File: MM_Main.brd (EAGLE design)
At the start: 74 x 87.2 mm, 81 parts, among them IC1 ULN2003AD, IC2 TB6612FNG, IC4 LD117ADT50TR, IC5 MCP1825, Q1 TEFT4300, Q2 TEFT4300, Q3 TEFT4300, Q4 TEFT4300, Q5 TEFT4300, Q6 TEFT4300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

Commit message: poprawione przyciski, kwarc i wylacznik zasilania
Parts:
- removed BT0, BT1, RST_BTN: TACTILE-SWITCH-7914G, GeekAmmo:7914G
- removed ZAS: (no value), special:EDG-01
- added Q8: 8MHz, _microMouse:CRYSTAL_5X3.2MM
- added S1: TL32PO, switch:TL3XPO
- added S2, S3: DTS-3, switch-tact:DTS-3
- added S4: DTSM-6, switch-tact:DTSM-6
- added S5: DTSM-3, switch-tact:DTSM-3
- added U$2: CRYSTAL_5X3.2MM, _microMouse:CRYSTAL_5X3.2MM
- C_OSC1, C_OSC2: value 27p -> 33p
- LED4: value green -> blue
- LED6: value yellow -> blue
- R10, R12, R13: value 10K -> 150R
- R11: value 10K -> 10k
- R20, R27: value 10K -> 33R
- R25: value (none) -> 10k
- moved Q7 37.0 mm to (42.6, 31.5)
- moved FUSE 13.6 mm to (-22.8, -32.2), turned to 180 degrees
- moved FUSE1 10.9 mm to (-22.8, -30.0), turned to 180 degrees
- moved LED3 4.58 mm to (28.4, -30.8), turned to 25 degrees
- moved LED2 2.01 mm to (29.2, -23.3), turned to 270 degrees
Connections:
- net +3V3: now also S3.1; no longer BT0.3
- net BTN: now also S2.1; no longer BT1.3
- net GND: now also S5.1; no longer RST_BTN.3
- net N$23: now also S3.2; no longer BT0.1
- net N$24: now also S1.2; no longer ZAS.2
- net N$29: now also S2.2; no longer BT1.1
- net N$9: now also S1.3; no longer ZAS.1
- net OSC_IN: now also Q8.P$2; no longer Q7.3
- net OSC_OUT: now also Q8.P$1; no longer Q7.1
- net RST: now also S5.2; no longer RST_BTN.1
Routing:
- net +7V: track 88.7 -> 75.3 mm
- net N$21: track 31.8 -> 24.8 mm
- net +3V3: track 345.6 -> 350.9 mm
- net N$23: track 32.6 -> 37.9 mm
- net N$24: track 5.84 -> 11.0 mm
- net LED2: track 59.5 -> 63.7 mm
- net BTN: track 71.8 -> 75.6 mm
- net OSC_IN: track 20.8 -> 17.6 mm, vias 2 -> 0
- net N$9: track 11.8 -> 8.63 mm
- net GND: track 468.3 -> 465.3 mm, vias 22 -> 20
- net N$8: track 22.5 -> 24.0 mm
- net LED1: track 57.1 -> 58.5 mm
- net N$29: track 25.2 -> 26.3 mm
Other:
- outline, holes or cut-outs redrawn
- board text removed: "BT0"
- board text removed: "BT1"
- board text removed: "BUZ1"
- board text removed: "C1"
- board text removed: "C12"
- board text removed: "C13"
- board text removed: "C15"
- board text removed: "C2"
- board text removed: "C21"
- board text removed: "C22"
- board text removed: "C3"
- board text removed: "C6"
- board text removed: "C_OSC1"
- board text removed: "C_OSC2"
- board text removed: "C_V1"
- board text removed: "C_V2"
- board text removed: "C_V3"
- board text removed: "C_VSSA"
- board text removed: "C_VSSA1"
- board text removed: "FUSE"
- board text removed: "IC1"
- board text removed: "IC2"
- board text removed: "IC4"
- board text removed: "IC5"
- board text removed: "LED1"
- board text removed: "LED2"
- board text removed: "LED3"
- board text removed: "LED4"
- board text removed: "LED6"
- board text removed: "R1"
- board text removed: "R10"
- board text removed: "R11"
- board text removed: "R12"
- board text removed: "R13"
- board text removed: "R15"
- board text removed: "R16"
- board text removed: "R17"
- board text removed: "R18"
- board text removed: "R19"
- board text removed: "R2"
- board text removed: "R20"
- board text removed: "R21"
- board text removed: "R22"
- board text removed: "R23"
- board text removed: "R24"
- board text removed: "R25"
- board text removed: "R26"
- board text removed: "R27"
- board text removed: "R3"
- board text removed: "R4"
- board text removed: "R5"
- board text removed: "R6"
- board text removed: "R7"
- board text removed: "R8"
- board text removed: "R9"
- board text removed: "RST_BTN"
- board text removed: "VCAP_1"
- board text removed: "VCAP_2"
- board text removed: "ZAS"

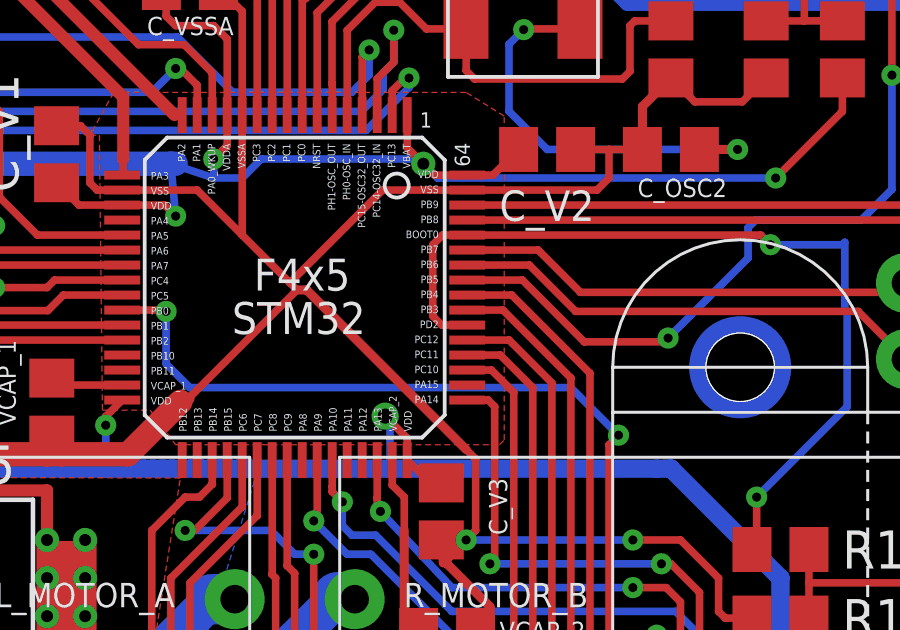
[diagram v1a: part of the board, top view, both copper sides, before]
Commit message: PD2 zamienione z PA15
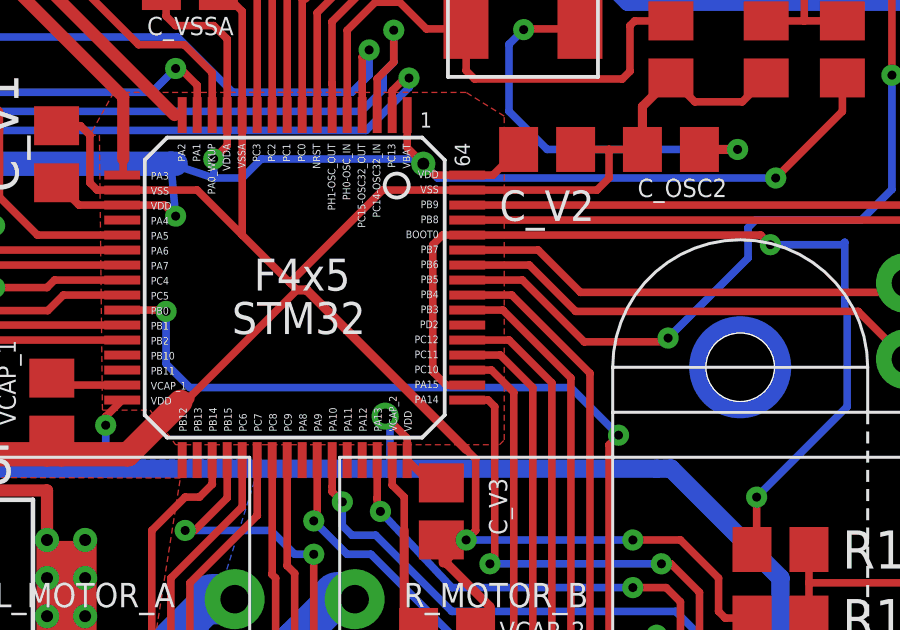
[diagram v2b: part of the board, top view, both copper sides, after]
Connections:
- net BOOT0: now also U$6.PA15; no longer U$6.PD2
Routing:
- net BOOT0: track 29.3 -> 31.2 mm
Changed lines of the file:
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@@
 <wire x1="5.75" y1="13.33875" x2="15.5347" y2="13.33875" width="0.254" layer="1"/>
 <wire x1="15.5347" y1="13.33875" x2="15.85595" y2="13.0175" width="0.254" layer="1"/>
-<contactref element="U$6" pad="PD2"/>
 <wire x1="5.75" y1="13.33875" x2="4.925" y2="13.33875" width="0.254" layer="1"/>
 <wire x1="4.925" y1="13.33875" x2="4.60375" y2="13.0175" width="0.254" layer="1"/>
-<wire x1="5.75" y1="10.33875" x2="4.90125" y2="10.33875" width="0.254" layer="1"/>
-<wire x1="4.90125" y1="10.33875" x2="4.60375" y2="10.63625" width="0.254" layer="1"/>
-<wire x1="4.60375" y1="10.63625" x2="4.60375" y2="13.0175" width="0.254" layer="1"/>
+<wire x1="4.60375" y1="8.78205" x2="4.60375" y2="13.0175" width="0.254" layer="1"/>
 <wire x1="15.2425" y1="2.8575" x2="15.39875" y2="3.01375" width="0.254" layer="1"/>
 <wire x1="15.39875" y1="3.01375" x2="15.39875" y2="4.60375" width="0.254" layer="1"/>
@@
 <wire x1="18.415" y1="10.795" x2="18.335625" y2="10.874375" width="0.254" layer="16"/>
 <wire x1="18.335625" y1="10.874375" x2="18.335625" y2="13.096875" width="0.254" layer="16"/>
+<contactref element="U$6" pad="PA15"/>
+<wire x1="5.75" y1="8.33875" x2="5.75" y2="8.3312" width="0.254" layer="1"/>
+<wire x1="5.75" y1="8.3312" x2="5.0546" y2="8.3312" width="0.254" layer="1"/>
+<wire x1="5.0546" y1="8.3312" x2="4.60375" y2="8.78205" width="0.254" layer="1"/>
 </signal>
 <signal name="N$23">

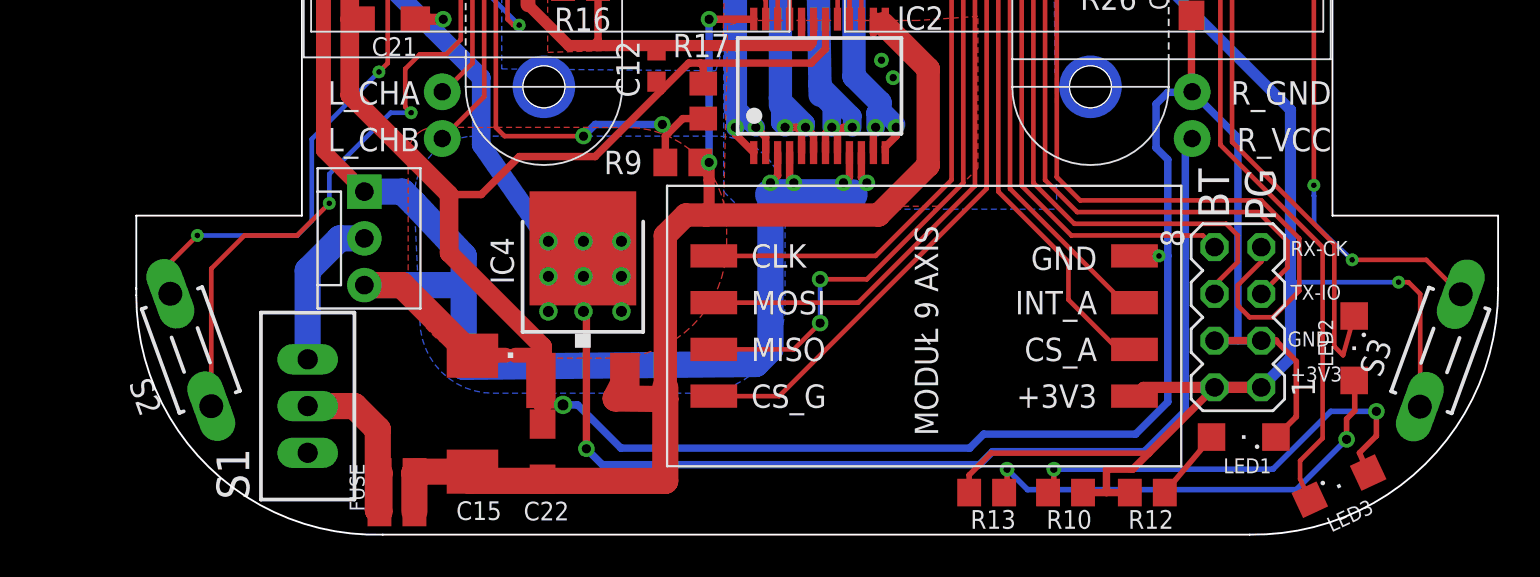
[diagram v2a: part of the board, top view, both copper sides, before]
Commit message: dodany suwak i miejsce na 2 lipo
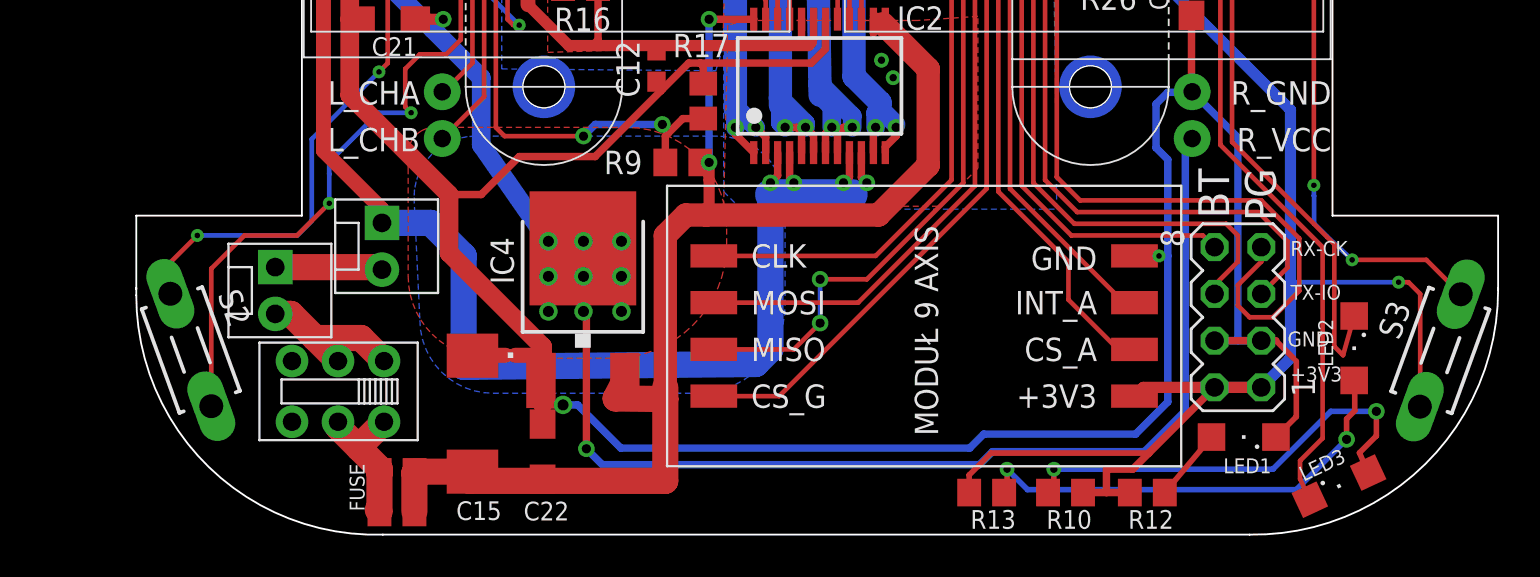
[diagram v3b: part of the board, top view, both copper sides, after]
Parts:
- removed JP1: (no value), SparkFun-Connectors:MOLEX-1X3
- removed S1: TL32PO, switch:TL3XPO
- added JP3, JP4: (no value), SparkFun_conn:MOLEX-1X2
- added U$3: PRZELACZNIK_SUWAKOWY, _microMouse:PRZELACZNIK_SUWAKOWY
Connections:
- new net N$36: JP3.2, U$3.2, U$3.3
- net GNDA: now also JP4.1; no longer JP1.1, JP1.3
- net N$24: now also U$3.5, U$3.6; no longer S1.2
- net N$9: now also JP3.1, JP4.2; no longer JP1.2, S1.3
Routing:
- net GNDA: track 116.6 -> 104.2 mm
- net N$36: track 0.00 -> 8.74 mm
- net N$24: track 11.0 -> 7.95 mm
- net N$9: track 8.63 -> 5.85 mm

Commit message: gerbery
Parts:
- removed Q7: 8MHz, crystal:CTS406
- removed S4: DTSM-6, switch-tact:DTSM-6
- removed U$2: CRYSTAL_5X3.2MM, _microMouse:CRYSTAL_5X3.2MM
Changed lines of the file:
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@@
 <grid distance="10" unitdist="mil" unit="mil" style="lines" multiple="1" display="yes" altdistance="1" altunitdist="mil" altunit="mil"/>
 <layers>
-<layer number="1" name="Top" color="4" fill="1" visible="yes" active="yes"/>
+<layer number="1" name="Top" color="4" fill="1" visible="no" active="yes"/>
 <layer number="2" name="Route2" color="1" fill="3" visible="no" active="no"/>
 <layer number="3" name="Route3" color="4" fill="3" visible="no" active="no"/>
@@
 <layer number="14" name="Route14" color="1" fill="6" visible="no" active="no"/>
 <layer number="15" name="Route15" color="4" fill="6" visible="no" active="no"/>
-<layer number="16" name="Bottom" color="1" fill="1" visible="yes" active="yes"/>
-<layer number="17" name="Pads" color="2" fill="1" visible="yes" active="yes"/>
-<layer number="18" name="Vias" color="2" fill="1" visible="yes" active="yes"/>
-<layer number="19" name="Unrouted" color="6" fill="1" visible="yes" active="yes"/>
-<layer number="20" name="Dimension" color="15" fill="1" visible="yes" active="yes"/>
+<layer number="16" name="Bottom" color="1" fill="1" visible="no" active="yes"/>
+<layer number="17" name="Pads" color="2" fill="1" visible="no" active="yes"/>
+<layer number="18" name="Vias" color="2" fill="1" visible="no" active="yes"/>
+<layer number="19" name="Unrouted" color="6" fill="1" visible="no" active="yes"/>
+<layer number="20" name="Dimension" color="15" fill="1" visible="no" active="yes"/>
 <layer number="21" name="tPlace" color="7" fill="1" visible="yes" active="yes"/>
-<layer number="22" name="bPlace" color="7" fill="1" visible="yes" active="yes"/>
-<layer number="23" name="tOrigins" color="15" fill="1" visible="yes" active="yes"/>
-<layer number="24" name="bOrigins" color="15" fill="1" visible="yes" active="yes"/>
+<layer number="22" name="bPlace" color="7" fill="1" visible="no" active="yes"/>
+<layer number="23" name="tOrigins" color="15" fill="1" visible="no" active="yes"/>
+<layer number="24" name="bOrigins" color="15" fill="1" visible="no" active="yes"/>
 <layer number="25" name="tNames" color="7" fill="1" visible="yes" active="yes"/>
-<layer number="26" name="bNames" color="7" fill="1" visible="yes" active="yes"/>
-<layer number="27" name="tValues" color="7" fill="1" visible="yes" active="yes"/>
-<layer number="28" name="bValues" color="7" fill="1" visible="yes" active="yes"/>
+<layer number="26" name="bNames" color="7" fill="1" visible="no" active="yes"/>
+<layer number="27" name="tValues" color="7" fill="1" visible="no" active="yes"/>
+<layer number="28" name="bValues" color="7" fill="1" visible="no" active="yes"/>
 <layer number="29" name="tStop" color="7" fill="3" visible="no" active="yes"/>
 <layer number="30" name="bStop" color="7" fill="6" visible="no" active="yes"/>
@@
 <element name="Q4" library="_MM" package="TEFT4300" value="TEFT4300" x="3.33375" y="49.05375" smashed="yes" rot="R308"/>
 <element name="Q3" library="_MM" package="TEFT4300" value="TEFT4300" x="-3.33375" y="49.05375" smashed="yes" rot="R52"/>
-<element name="Q7" library="crystal" package="CTS406" value="8MHz" x="42.62" y="31.4945" smashed="yes" rot="R180">
-<attribute name="OC_NEWARK" value="unknown" x="42.62" y="31.4945" size="1.778" layer="27" rot="R180" display="off"/>
-<attribute name="MPN" value="" x="42.62" y="31.4945" size="1.778" layer="27" rot="R180" display="off"/>
-<attribute name="MF" value="" x="42.62" y="31.4945" size="1.778" layer="27" rot="R180" display="off"/>
-<attribute name="OC_FARNELL" value="unknown" x="42.62" y="31.4945" size="1.778" layer="27" rot="R180" display="off"/>
-<attribute name="VALUE" x="45.16" y="35.3045" size="1.27" layer="27" rot="R180"/>
-</element>
 <element name="R1" library="rcl" package="R0805" value="" x="20.5994" y="25.48255" smashed="yes" rot="R180">
 <attribute name="NAME" x="18.85315" y="26.11755" size="1.27" layer="25" rot="R180"/>
@@
 <attribute name="VALUE" x="15.5575" y="-4.1275" size="1.27" layer="27"/>
 </element>
-<element name="U$2" library="_microMouse" package="CRYSTAL_5X3.2MM" value="CRYSTAL_5X3.2MM" x="-265.18405" y="0"/>
 <element name="Q8" library="_microMouse" package="CRYSTAL_5X3.2MM" value="8MHz" x="7.4092" y="20.0818"/>
 <element name="S2" library="switch-tact" package="DTS-3" value="DTS-3" x="-34.036" y="-23.368" smashed="yes" rot="R110">
@@
 <attribute name="VALUE" x="37.839696875" y="-27.591315625" size="1.27" layer="27" rot="R70" display="off"/>
 </element>
-<element name="S4" library="switch-tact" package="DTSM-6" value="DTSM-6" x="37.338" y="45.212"/>
 <element name="S5" library="switch-tact" package="DTSM-3" value="DTSM-3" x="0" y="24.13"/>
 <element name="JP3" library="SparkFun_conn" package="MOLEX-1X2" value="" x="-29.4492" y="-18.8658" smashed="yes" rot="R270"/>

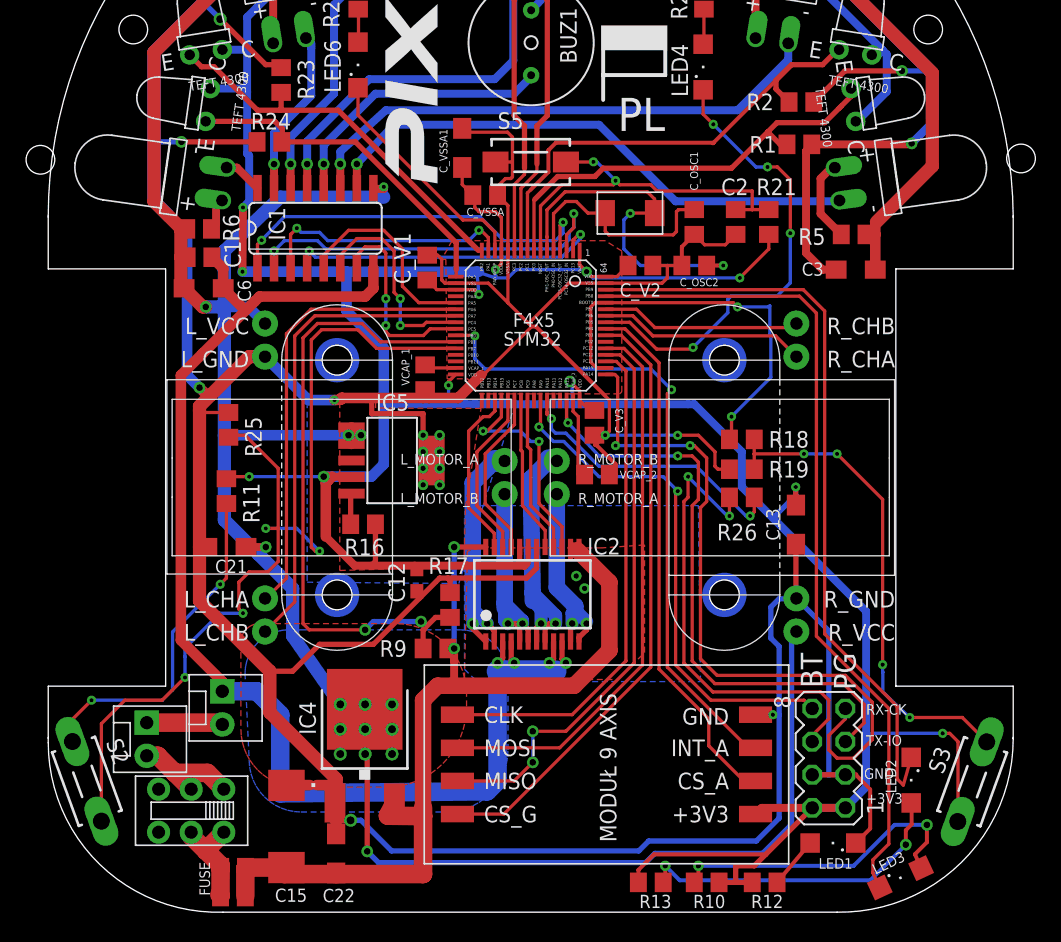
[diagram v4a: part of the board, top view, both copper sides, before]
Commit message: to 2 gniazdo moze szorowac o kolo... zmienilem tez konfiguuracje power-switcha, bo tak patrzac na strone electro-parku to tak odczyruje ta konfiguracje, zrobilem drc
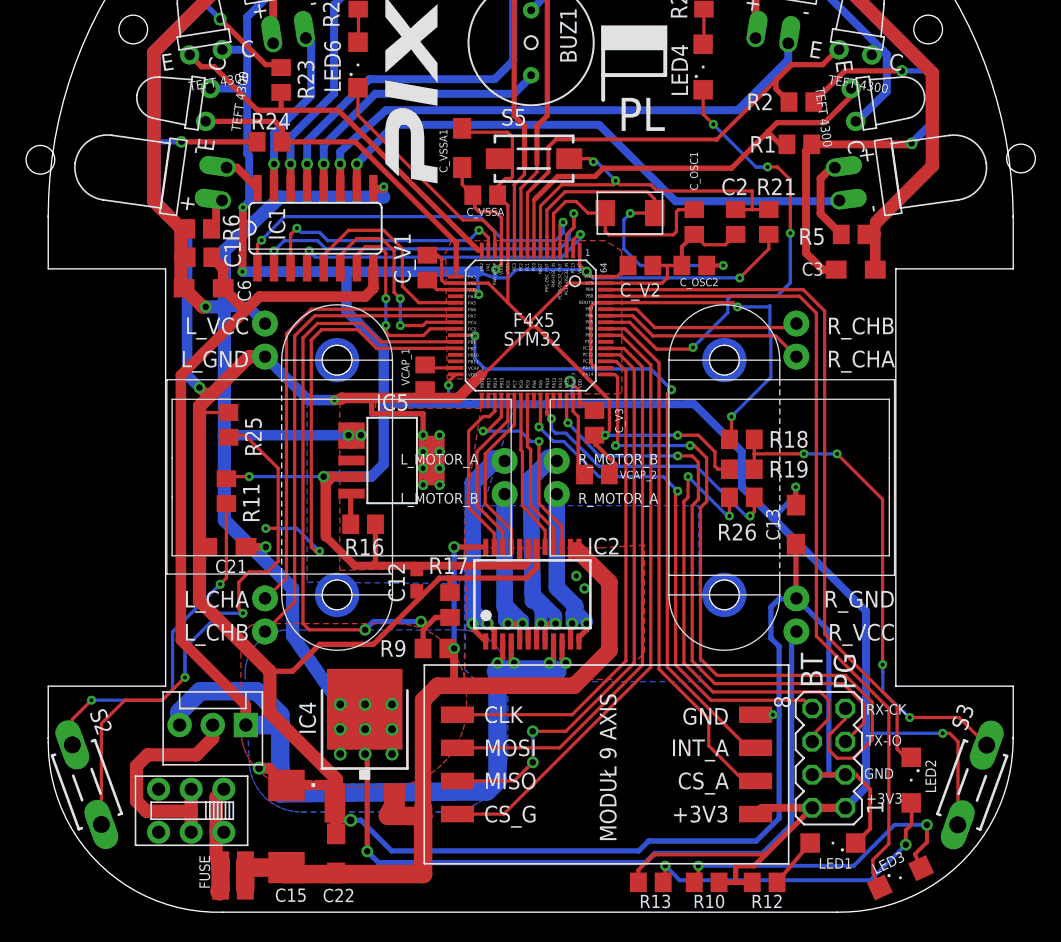
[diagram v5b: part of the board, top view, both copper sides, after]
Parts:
- removed JP3, JP4: (no value), SparkFun_conn:MOLEX-1X2
- added JP1: (no value), SparkFun-Connectors:MOLEX-1X3
- moved FUSE 0.51 mm to (-22.8, -31.6)
- moved FUSE1 0.51 mm to (-22.8, -29.5)
- moved S5 0.36 mm to (0.25, 24.4)
- moved S2 0.25 mm to (-34.0, -23.6)
- moved S3 0.25 mm to (33.9, -23.6)
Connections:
- removed net N$9: JP3.1, JP4.2
- net GNDA: now also JP1.1, JP1.3; no longer JP4.1
- net N$24: now also U$3.3; no longer U$3.5
- net N$36: now also JP1.2, U$3.5; no longer JP3.2, U$3.3
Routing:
- net GNDA: track 104.2 -> 119.5 mm, vias 6 -> 7
- net N$36: track 8.74 -> 18.2 mm
- net N$9: track 5.85 -> 0.00 mm
- net LED1: track 58.5 -> 54.7 mm
- net N$24: track 7.95 -> 9.19 mm

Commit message: drobne poprawki, chyba koniec :P
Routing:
- net +5V: track 296.5 -> 298.1 mm
- net GND: track 465.0 -> 466.4 mm
- net BTN: track 76.3 -> 75.7 mm
